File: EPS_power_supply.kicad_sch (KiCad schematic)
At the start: 15 parts, among them IC1 TPS7B8733QDDARQ1, IC2 TPS7B8750QDDARQ1

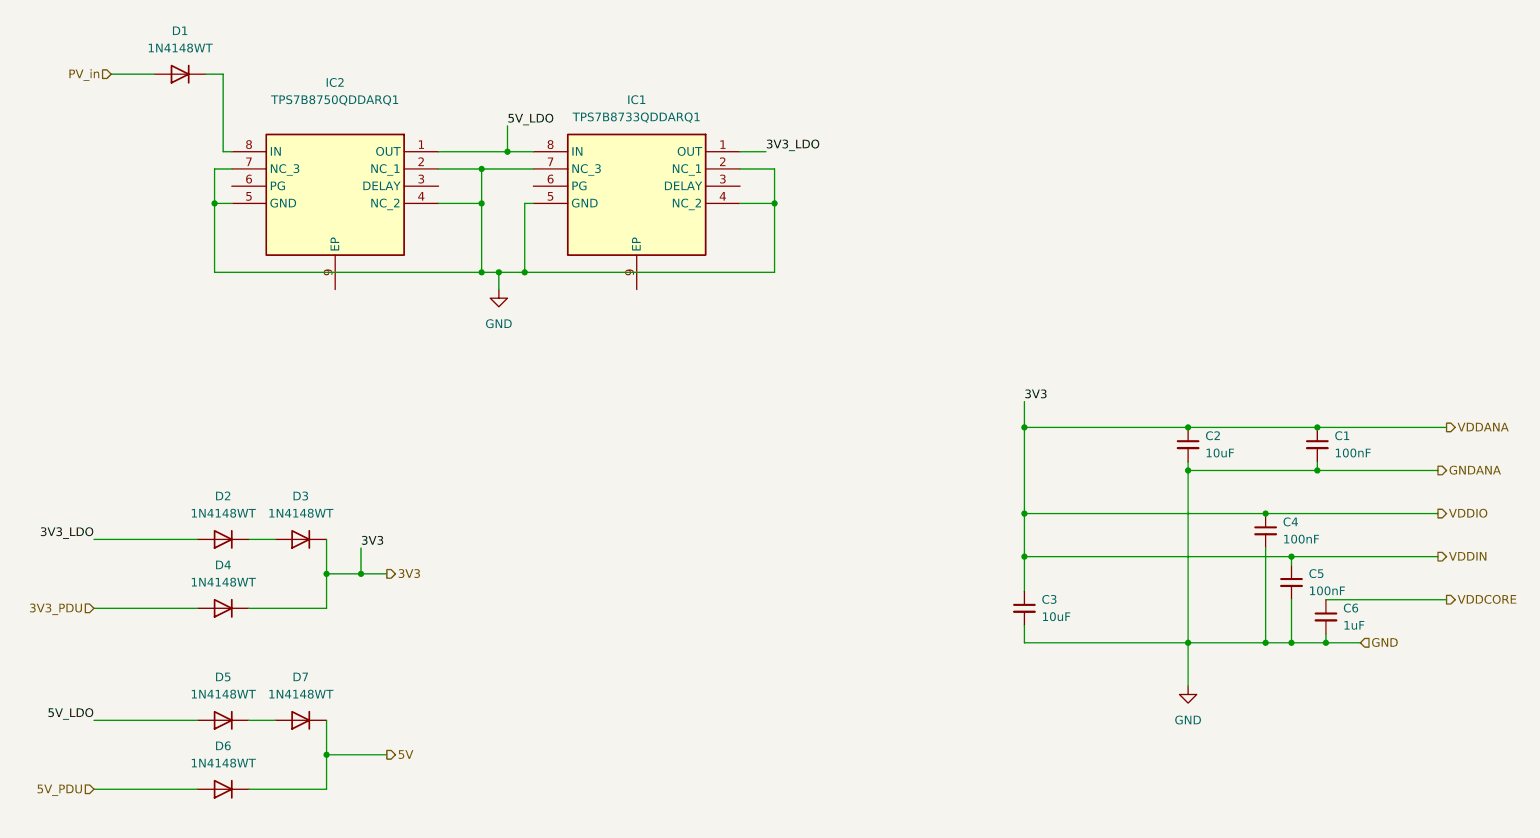
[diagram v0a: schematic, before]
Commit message: small power supply modification
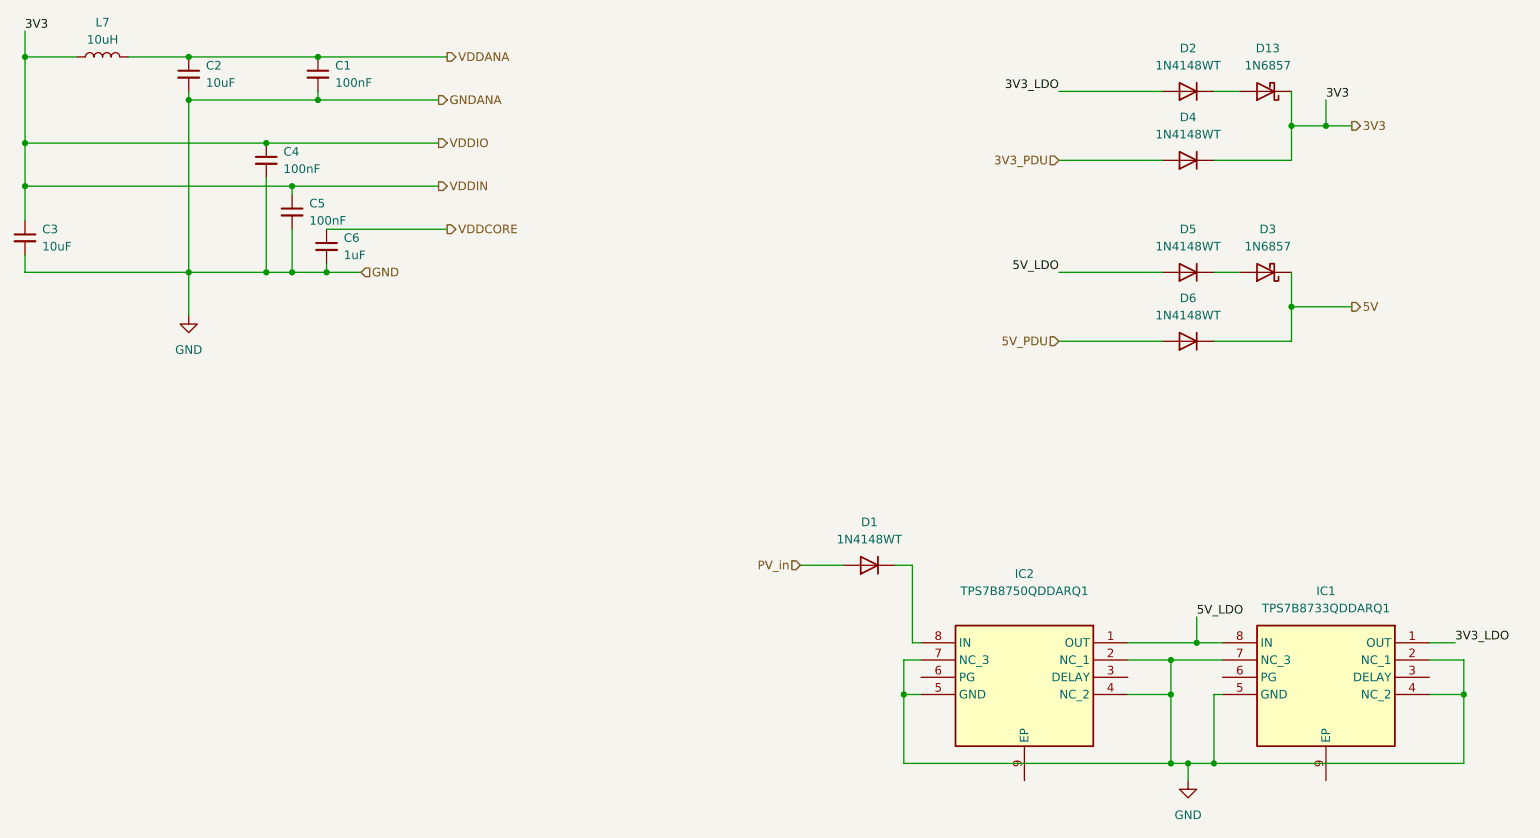
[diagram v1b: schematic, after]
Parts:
- removed D3, D7: 1N4148WT, Diode_SMD:D_SOD-523, symbol Diode:1N4148WT
- added D13, D3: 1N6857, Diode_SMD:D_SOD-323, symbol Diode:1N6857
- added L7: 10uH, symbol Device:L
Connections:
- net 3V3: now also D13.1 (K), L7.1; no longer C1.1, C2.1
- net 5V: now also D3.1 (K)
- net at D5.1 (K): now also D3.2 (A)
- net at D2.1 (K): now also D13.2 (A)
- new net VDDANA: C1.1, C2.1, L7.2
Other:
- moved on the sheet: C1, C2, C3, C4, C5, C6, D1, D2, D4, D5, D6, IC1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
